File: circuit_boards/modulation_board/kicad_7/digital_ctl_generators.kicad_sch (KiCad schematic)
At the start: 0 parts

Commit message: Progress on circuit boards
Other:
- sheet DAC ports: added VOLUME_CV; removed MIDI_VCF_FREQ
- sheet microcontroller ports: added none; removed GATE
- note added: "[-1.25v, +1.25v]"
- note added: "[-5v, +5v]"
- note added: "[0v, 10v]"
- note added: "[0v, 2.5v]"

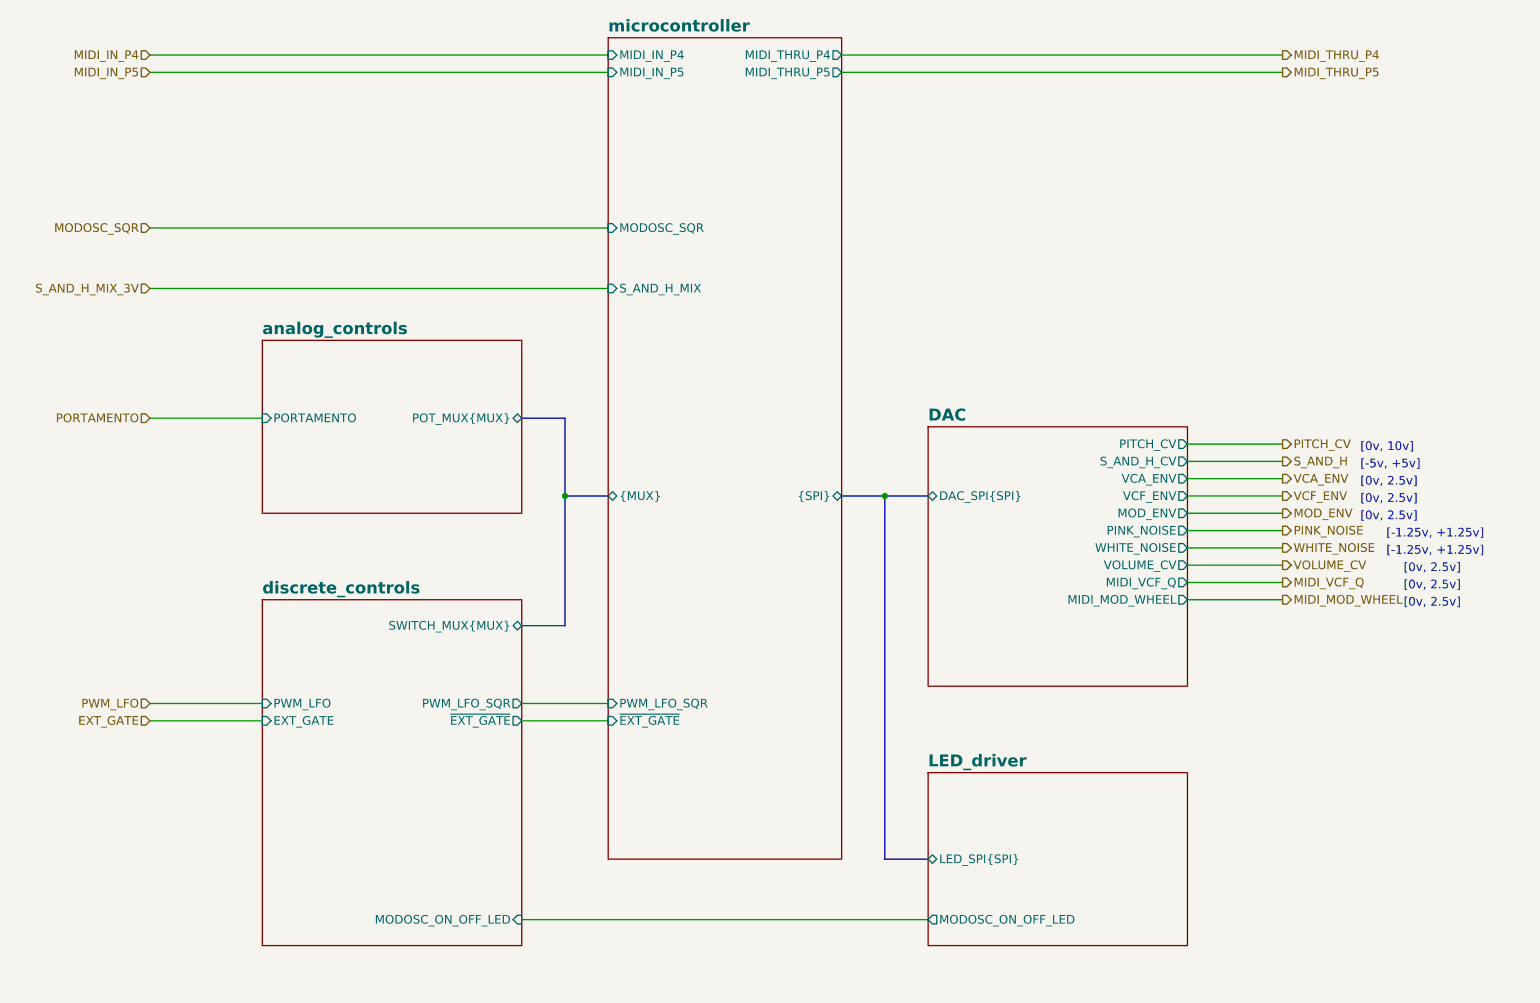
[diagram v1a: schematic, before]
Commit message: Tweaks to mod board, debounce MODOSC toggle switch
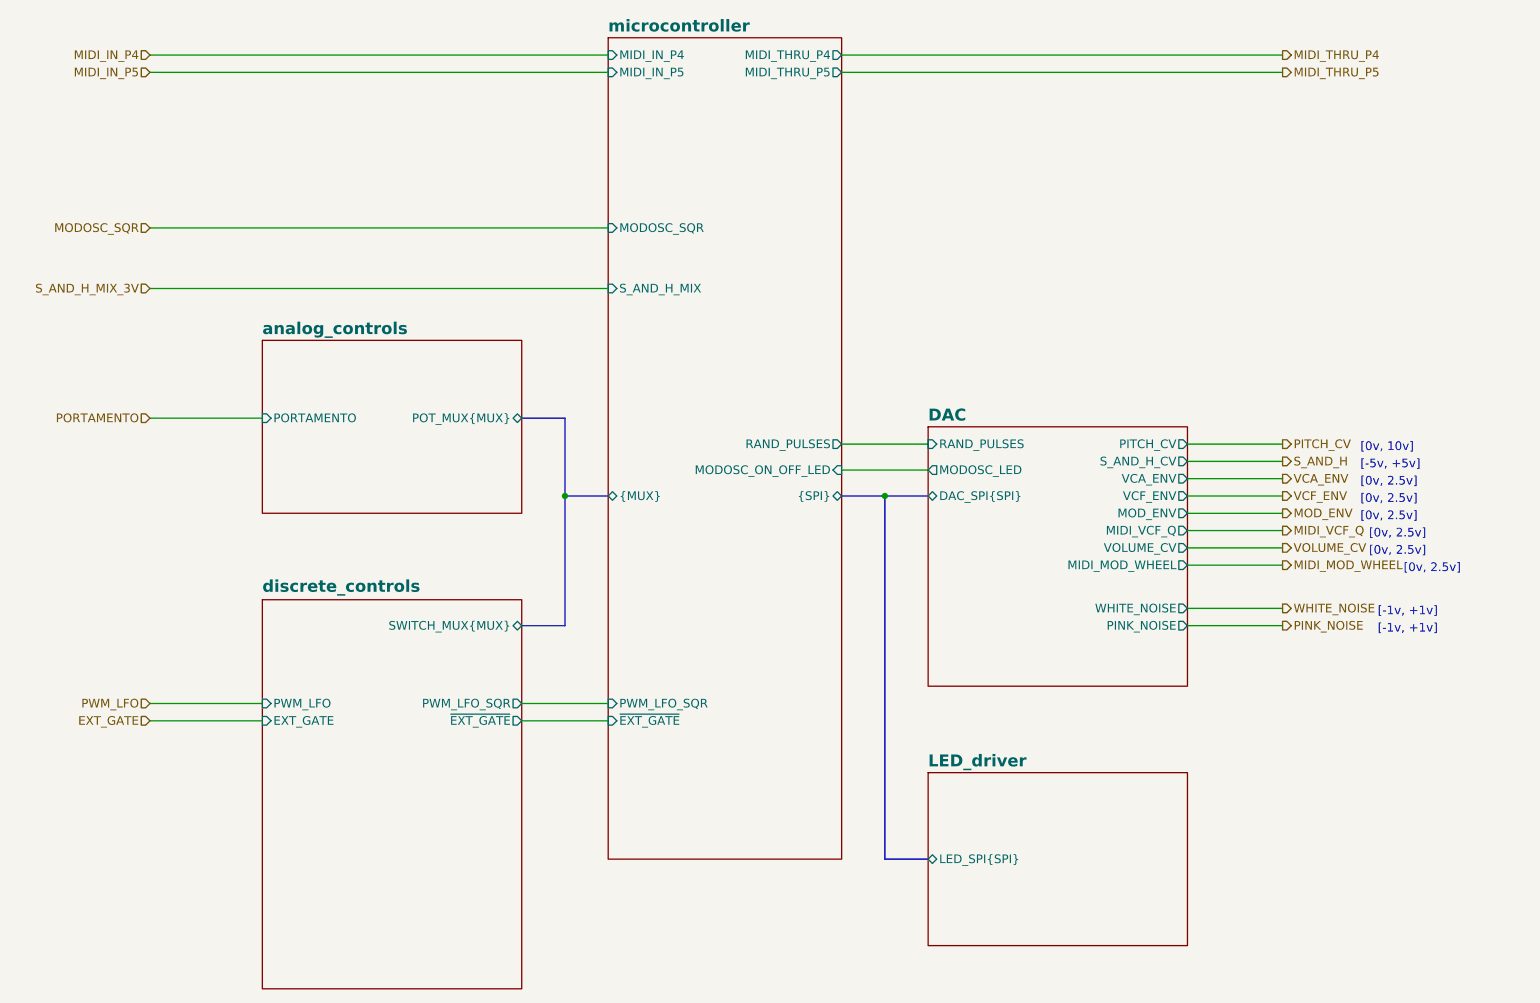
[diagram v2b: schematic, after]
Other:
- sheet DAC ports: added MODOSC_LED, RAND_PULSES; removed none
- sheet LED_driver ports: added none; removed MODOSC_ON_OFF_LED
- sheet discrete_controls ports: added none; removed MODOSC_ON_OFF_LED
- sheet microcontroller ports: added MODOSC_ON_OFF_LED, RAND_PULSES; removed none
- note added: "[-1v, +1v]"
- note removed: "[-1.25v, +1.25v]"
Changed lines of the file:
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@@
   (title_block
     (title "MICRO-OX Modulation Board")
-    (date "2023-04-13")
+    (date "2023-04-20")
     (rev "0")
     (comment 2 "creativecommons.org/licenses/by/4.0")
@@
     (stroke (width 0) (type default))
   )
+  (wire (pts (xy 165.1 90.17) (xy 177.8 90.17))
+    (stroke (width 0) (type default))
+  )
   (wire (pts (xy 63.5 63.5) (xy 130.81 63.5))
     (stroke (width 0) (type default))
@@
     (stroke (width 0) (type default))
   )
+  (wire (pts (xy 215.9 113.03) (xy 229.87 113.03))
+    (stroke (width 0) (type default))
+  )
   (wire (pts (xy 63.5 124.46) (xy 80.01 124.46))
     (stroke (width 0) (type default))
@@
     (stroke (width 0) (type default))
   )
+  (wire (pts (xy 215.9 99.06) (xy 229.87 99.06))
+    (stroke (width 0) (type default))
+  )
+  (bus (pts (xy 165.1 93.98) (xy 171.45 93.98))
+    (stroke (width 0) (type default))
+  )
+  (wire (pts (xy 63.5 82.55) (xy 80.01 82.55))
+    (stroke (width 0) (type default))
+  )
   (wire (pts (xy 215.9 101.6) (xy 229.87 101.6))
     (stroke (width 0) (type default))
   )
-  (wire (pts (xy 215.9 106.68) (xy 229.87 106.68))
-    (stroke (width 0) (type default))
-  )
-  (bus (pts (xy 165.1 93.98) (xy 171.45 93.98))
-    (stroke (width 0) (type default))
-  )
-  (wire (pts (xy 63.5 82.55) (xy 80.01 82.55))
-    (stroke (width 0) (type default))
-  )
-  (wire (pts (xy 215.9 99.06) (xy 229.87 99.06))
+  (bus (pts (xy 118.11 113.03) (xy 124.46 113.03))
+    (stroke (width 0) (type default))
+  )
+  (wire (pts (xy 215.9 110.49) (xy 229.87 110.49))
+    (stroke (width 0) (type default))
+  )
+  (wire (pts (xy 165.1 86.36) (xy 177.8 86.36))
+    (stroke (width 0) (type default))
+  )
+  (wire (pts (xy 63.5 31.75) (xy 130.81 31.75))
+    (stroke (width 0) (type default))
+  )
+  (bus (pts (xy 124.46 93.98) (xy 124.46 82.55))
+    (stroke (width 0) (type default))
+  )
+  (wire (pts (xy 215.9 86.36) (xy 229.87 86.36))
+    (stroke (width 0) (type default))
+  )
+  (wire (pts (xy 165.1 29.21) (xy 229.87 29.21))
+    (stroke (width 0) (type default))
+  )
+  (bus (pts (xy 171.45 93.98) (xy 171.45 147.32))
+    (stroke (width 0) (type default))
+  )
+  (wire (pts (xy 215.9 88.9) (xy 229.87 88.9))
+    (stroke (width 0) (type default))
+  )
+  (wire (pts (xy 118.11 124.46) (xy 130.81 124.46))
     (stroke (width 0) (type default))
   )
@@
     (stroke (width 0) (type default))
   )
-  (wire (pts (xy 118.11 156.21) (xy 177.8 156.21))
-    (stroke (width 0) (type default))
-  )
-  (bus (pts (xy 118.11 113.03) (xy 124.46 113.03))
-    (stroke (width 0) (type default))
-  )
-  (wire (pts (xy 63.5 31.75) (xy 130.81 31.75))
-    (stroke (width 0) (type default))
-  )
-  (bus (pts (xy 124.46 93.98) (xy 124.46 82.55))
-    (stroke (width 0) (type default))
-  )
-  (wire (pts (xy 215.9 86.36) (xy 229.87 86.36))
-    (stroke (width 0) (type default))
-  )
-  (wire (pts (xy 165.1 29.21) (xy 229.87 29.21))
-    (stroke (width 0) (type default))
-  )
-  (bus (pts (xy 171.45 93.98) (xy 171.45 147.32))
-    (stroke (width 0) (type default))
-  )
-  (wire (pts (xy 215.9 88.9) (xy 229.87 88.9))
-    (stroke (width 0) (type default))
-  )
-  (wire (pts (xy 118.11 124.46) (xy 130.81 124.46))
-    (stroke (width 0) (type default))
-  )
-  (wire (pts (xy 215.9 109.22) (xy 229.87 109.22))
-    (stroke (width 0) (type default))
-  )
   (bus (pts (xy 171.45 93.98) (xy 177.8 93.98))
     (stroke (width 0) (type default))
@@
     (stroke (width 0) (type default))
   )
-  (text "[-1.25v, +1.25v]" (at 245.11 102.87 0)
-    (effects (font (size 1.27 1.27)) (justify left bottom))
-  )
-  (text "[0v, 2.5v]" (at 247.65 107.95 0)
+  (text "[0v, 2.5v]" (at 242.57 100.33 0)
+    (effects (font (size 1.27 1.27)) (justify left bottom))
+  )
+  (text "[-1v, +1v]" (at 243.84 114.3 0)
     (effects (font (size 1.27 1.27)) (justify left bottom))
   )
@@
     (effects (font (size 1.27 1.27)) (justify left bottom))
   )
-  (text "[0v, 2.5v]" (at 247.65 110.49 0)
+  (text "[0v, 2.5v]" (at 247.65 105.41 0)
+    (effects (font (size 1.27 1.27)) (justify left bottom))
+  )
+  (text "[-1v, +1v]" (at 243.84 111.76 0)
     (effects (font (size 1.27 1.27)) (justify left bottom))
   )
@@
     (effects (font (size 1.27 1.27)) (justify left bottom))
   )
-  (text "[0v, 2.5v]" (at 247.65 105.41 0)
-    (effects (font (size 1.27 1.27)) (justify left bottom))
-  )
-  (text "[-1.25v, +1.25v]" (at 245.11 100.33 0)
+  (text "[0v, 2.5v]" (at 242.57 102.87 0)
     (effects (font (size 1.27 1.27)) (justify left bottom))
   )
@@
     (effects (font (size 1.27 1.27)) (justify left))
   )
+  (hierarchical_label "WHITE_NOISE" (shape output) (at 229.87 110.49 0) (fields_autoplaced)
+    (effects (font (size 1.27 1.27)) (justify left))
+  )
   (hierarchical_label "MIDI_IN_P4" (shape input) (at 63.5 29.21 180) (fields_autoplaced)
     (effects (font (size 1.27 1.27)) (justify right))
@@
     (effects (font (size 1.27 1.27)) (justify left))
   )
-  (hierarchical_label "VOLUME_CV" (shape output) (at 229.87 104.14 0) (fields_autoplaced)
+  (hierarchical_label "VOLUME_CV" (shape output) (at 229.87 101.6 0) (fields_autoplaced)
     (effects (font (size 1.27 1.27)) (justify left))
   )
@@
     (effects (font (size 1.27 1.27)) (justify right))
   )
+  (hierarchical_label "PINK_NOISE" (shape output) (at 229.87 113.03 0) (fields_autoplaced)
+    (effects (font (size 1.27 1.27)) (justify left))
+  )
   (hierarchical_label "S_AND_H_MIX_3V" (shape input) (at 63.5 63.5 180) (fields_autoplaced)
     (effects (font (size 1.27 1.27)) (justify right))
@@
     (effects (font (size 1.27 1.27)) (justify right))
   )
-  (hierarchical_label "WHITE_NOISE" (shape output) (at 229.87 101.6 0) (fields_autoplaced)
-    (effects (font (size 1.27 1.27)) (justify left))
-  )
   (hierarchical_label "VCF_ENV" (shape output) (at 229.87 93.98 0) (fields_autoplaced)
     (effects (font (size 1.27 1.27)) (justify left))
@@
     (effects (font (size 1.27 1.27)) (justify left))
   )
-  (hierarchical_label "MIDI_VCF_Q" (shape output) (at 229.87 106.68 0) (fields_autoplaced)
+  (hierarchical_label "MIDI_VCF_Q" (shape output) (at 229.87 99.06 0) (fields_autoplaced)
     (effects (font (size 1.27 1.27)) (justify left))
   )
@@
     (effects (font (size 1.27 1.27)) (justify left))
   )
-  (hierarchical_label "PINK_NOISE" (shape output) (at 229.87 99.06 0) (fields_autoplaced)
-    (effects (font (size 1.27 1.27)) (justify left))
-  )
-  (hierarchical_label "MIDI_MOD_WHEEL" (shape output) (at 229.87 109.22 0) (fields_autoplaced)
+  (hierarchical_label "MIDI_MOD_WHEEL" (shape output) (at 229.87 104.14 0) (fields_autoplaced)
     (effects (font (size 1.27 1.27)) (justify left))
   )
@@
       (effects (font (size 1.27 1.27)) (justify left))
     )
-    (pin "MODOSC_ON_OFF_LED" output (at 177.8 156.21 180)
-      (effects (font (size 1.27 1.27)) (justify left))
-    )
     (instances
       (project "modulation_board"
@@
     )
   )
-  (sheet (at 80.01 109.22) (size 38.1 50.8) (fields_autoplaced)
-    (stroke (width 0.1524) (type solid))
-    (fill (color 0 0 0 0.0000))
-    (property "Sheetname" "discrete_controls" (at 80.01 108.5084 0)
-      (effects (font (size 1.75 1.75) bold) (justify left bottom))
-    )
-    (property "Sheetfile" "discrete_controls.kicad_sch" (at 80.01 160.6046 0)
+  (sheet (at 80.01 109.22) (size 38.1 57.15) (fields_autoplaced)
+    (stroke (width 0.1524) (type solid))
+    (fill (color 0 0 0 0.0000))
+    (property "Sheetname" "discrete_controls" (at 80.01 108.2684 0)
+      (effects (font (size 1.75 1.75) bold) (justify left bottom))
+    )
+    (property "Sheetfile" "discrete_controls.kicad_sch" (at 80.01 166.9546 0)
       (effects (font (size 1.27 1.27)) (justify left top) hide)
     )
     (pin "SWITCH_MUX{MUX}" bidirectional (at 118.11 113.03 0)
-      (effects (font (size 1.27 1.27)) (justify right))
-    )
-    (pin "MODOSC_ON_OFF_LED" input (at 118.11 156.21 0)
       (effects (font (size 1.27 1.27)) (justify right))
     )
@@
       (effects (font (size 1.27 1.27)) (justify left))
     )
+    (pin "RAND_PULSES" output (at 165.1 86.36 0)
+      (effects (font (size 1.27 1.27)) (justify right))
+    )
+    (pin "MODOSC_ON_OFF_LED" input (at 165.1 90.17 0)
+      (effects (font (size 1.27 1.27)) (justify right))
+    )
     (instances
       (project "modulation_board"
@@
       (effects (font (size 1.27 1.27)) (justify right))
     )
-    (pin "PINK_NOISE" output (at 215.9 99.06 0)
-      (effects (font (size 1.27 1.27)) (justify right))
-    )
-    (pin "WHITE_NOISE" output (at 215.9 101.6 0)
-      (effects (font (size 1.27 1.27)) (justify right))
-    )
-    (pin "MIDI_MOD_WHEEL" output (at 215.9 109.22 0)
-      (effects (font (size 1.27 1.27)) (justify right))
-    )
-    (pin "MIDI_VCF_Q" output (at 215.9 106.68 0)
-      (effects (font (size 1.27 1.27)) (justify right))
-    )
-    (pin "VOLUME_CV" output (at 215.9 104.14 0)
-      (effects (font (size 1.27 1.27)) (justify right))
-    )
-    (instances
+    (pin "MIDI_MOD_WHEEL" output (at 215.9 104.14 0)
+      (effects (font (size 1.27 1.27)) (justify right))
+    )
+    (pin "MIDI_VCF_Q" output (at 215.9 99.06 0)
+      (effects (font (size 1.27 1.27)) (justify right))
+    )
+    (pin "VOLUME_CV" output (at 215.9 101.6 0)
+      (effects (font (size 1.27 1.27)) (justify right))
+    )
+    (pin "MODOSC_LED" output (at 177.8 90.17 180)
+      (effects (font (size 1.27 1.27)) (justify left))
+    )
+    (pin "PINK_NOISE" output (at 215.9 113.03 0)
+      (effects (font (size 1.27 1.27)) (justify right))
+    )
+    (pin "WHITE_NOISE" output (at 215.9 110.49 0)
+      (effects (font (size 1.27 1.27)) (justify right))
+    )
+    (pin "RAND_PULSES" input (at 177.8 86.36 180)
+      (effects (font (size 1.27 1.27)) (justify left))
+    )
+    (instances

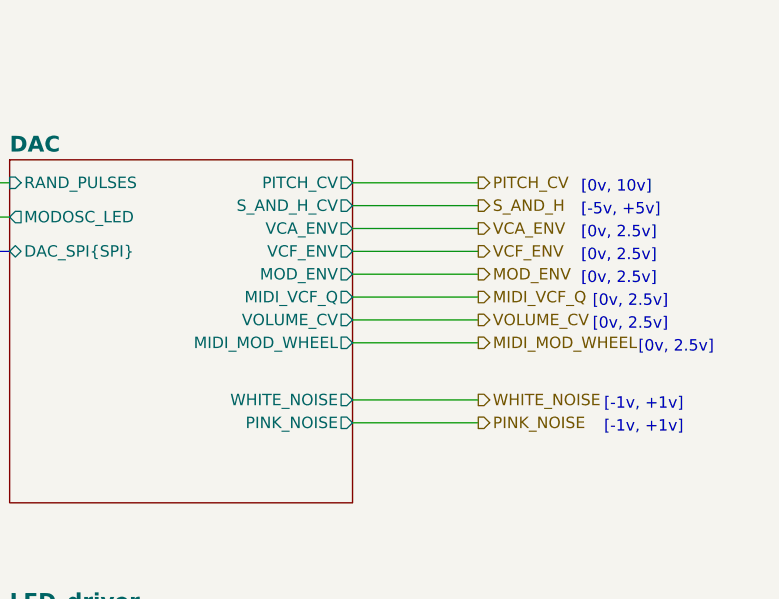
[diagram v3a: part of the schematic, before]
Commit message: Update PCBs, tweak vals, add VCF CV from DAC
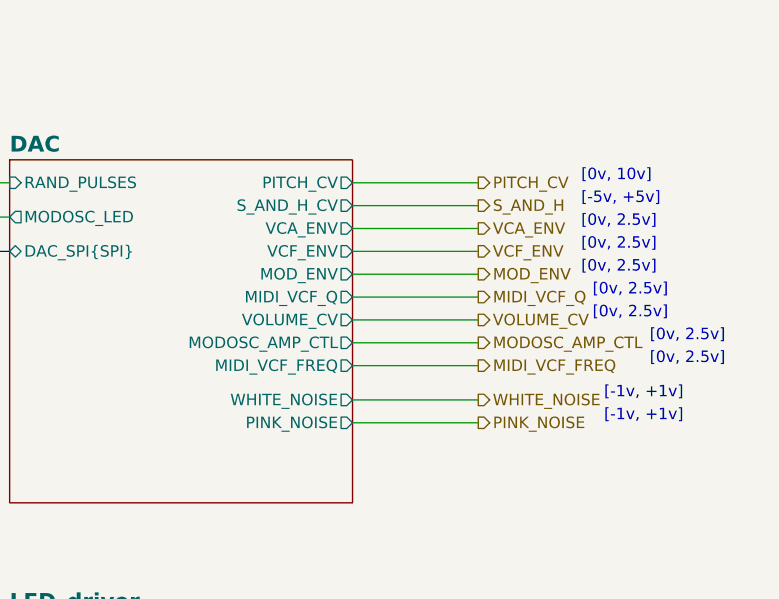
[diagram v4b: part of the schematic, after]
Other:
- sheet DAC ports: added MIDI_VCF_FREQ, MODOSC_AMP_CTL; removed MIDI_MOD_WHEEL
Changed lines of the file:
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@@
   (title_block
     (title "MICRO-OX Modulation Board")
-    (date "2023-04-21")
+    (date "2023-04-25")
     (rev "0")
     (comment 2 "creativecommons.org/licenses/by/4.0")
@@
     (stroke (width 0) (type default))
   )
+  (wire (pts (xy 215.9 106.68) (xy 229.87 106.68))
+    (stroke (width 0) (type default))
+  )
   (wire (pts (xy 215.9 99.06) (xy 229.87 99.06))
     (stroke (width 0) (type default))
@@
     (stroke (width 0) (type default))
   )
-  (text "[0v, 2.5v]" (at 242.57 100.33 0)
-    (effects (font (size 1.27 1.27)) (justify left bottom))
-  )
-  (text "[-1v, +1v]" (at 243.84 114.3 0)
-    (effects (font (size 1.27 1.27)) (justify left bottom))
-  )
-  (text "[0v, 2.5v]" (at 241.3 92.71 0)
-    (effects (font (size 1.27 1.27)) (justify left bottom))
-  )
-  (text "[-5v, +5v]" (at 241.3 90.17 0)
-    (effects (font (size 1.27 1.27)) (justify left bottom))
-  )
-  (text "[0v, 2.5v]" (at 247.65 105.41 0)
-    (effects (font (size 1.27 1.27)) (justify left bottom))
-  )
-  (text "[-1v, +1v]" (at 243.84 111.76 0)
-    (effects (font (size 1.27 1.27)) (justify left bottom))
-  )
-  (text "[0v, 2.5v]" (at 241.3 97.79 0)
-    (effects (font (size 1.27 1.27)) (justify left bottom))
-  )
-  (text "[0v, 2.5v]" (at 242.57 102.87 0)
-    (effects (font (size 1.27 1.27)) (justify left bottom))
-  )
-  (text "[0v, 2.5v]" (at 241.3 95.25 0)
-    (effects (font (size 1.27 1.27)) (justify left bottom))
-  )
-  (text "[0v, 10v]" (at 241.3 87.63 0)
+  (text "[0v, 2.5v]" (at 242.57 99.06 0)
+    (effects (font (size 1.27 1.27)) (justify left bottom))
+  )
+  (text "[-1v, +1v]" (at 243.84 113.03 0)
+    (effects (font (size 1.27 1.27)) (justify left bottom))
+  )
+  (text "[0v, 2.5v]" (at 241.3 91.44 0)
+    (effects (font (size 1.27 1.27)) (justify left bottom))
+  )
+  (text "[-5v, +5v]" (at 241.3 88.9 0)
+    (effects (font (size 1.27 1.27)) (justify left bottom))
+  )
+  (text "[0v, 2.5v]" (at 248.92 104.14 0)
+    (effects (font (size 1.27 1.27)) (justify left bottom))
+  )
+  (text "[-1v, +1v]" (at 243.84 110.49 0)
+    (effects (font (size 1.27 1.27)) (justify left bottom))
+  )
+  (text "[0v, 2.5v]" (at 241.3 96.52 0)
+    (effects (font (size 1.27 1.27)) (justify left bottom))
+  )
+  (text "[0v, 2.5v]" (at 242.57 101.6 0)
+    (effects (font (size 1.27 1.27)) (justify left bottom))
+  )
+  (text "[0v, 2.5v]" (at 248.92 106.68 0)
+    (effects (font (size 1.27 1.27)) (justify left bottom))
+  )
+  (text "[0v, 2.5v]" (at 241.3 93.98 0)
+    (effects (font (size 1.27 1.27)) (justify left bottom))
+  )
+  (text "[0v, 10v]" (at 241.3 86.36 0)
     (effects (font (size 1.27 1.27)) (justify left bottom))
   )
@@
     (effects (font (size 1.27 1.27)) (justify right))
   )
+  (hierarchical_label "MIDI_VCF_FREQ" (shape output) (at 229.87 106.68 0) (fields_autoplaced)
+    (effects (font (size 1.27 1.27)) (justify left))
+  )
   (hierarchical_label "MODOSC_SQR" (shape input) (at 63.5 54.61 180) (fields_autoplaced)
     (effects (font (size 1.27 1.27)) (justify right))
@@
     (effects (font (size 1.27 1.27)) (justify left))
   )
-  (hierarchical_label "MIDI_MOD_WHEEL" (shape output) (at 229.87 104.14 0) (fields_autoplaced)
+  (hierarchical_label "MODOSC_AMP_CTL" (shape output) (at 229.87 104.14 0) (fields_autoplaced)
     (effects (font (size 1.27 1.27)) (justify left))
   )
@@
       (effects (font (size 1.27 1.27)) (justify right))
     )
-    (pin "MIDI_MOD_WHEEL" output (at 215.9 104.14 0)
-      (effects (font (size 1.27 1.27)) (justify right))
-    )
     (pin "MIDI_VCF_Q" output (at 215.9 99.06 0)
       (effects (font (size 1.27 1.27)) (justify right))
@@
       (effects (font (size 1.27 1.27)) (justify left))
     )
-    (instances
+    (pin "MODOSC_AMP_CTL" output (at 215.9 104.14 0)
+      (effects (font (size 1.27 1.27)) (justify right))
+    )
+    (pin "MIDI_VCF_FREQ" output (at 215.9 106.68 0)
+      (effects (font (size 1.27 1.27)) (justify right))
+    )
+    (instances
